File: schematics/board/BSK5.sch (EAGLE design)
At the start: 88 parts, among them U1 STM32F405RGT6, X1 JST-6, X11 JST-6

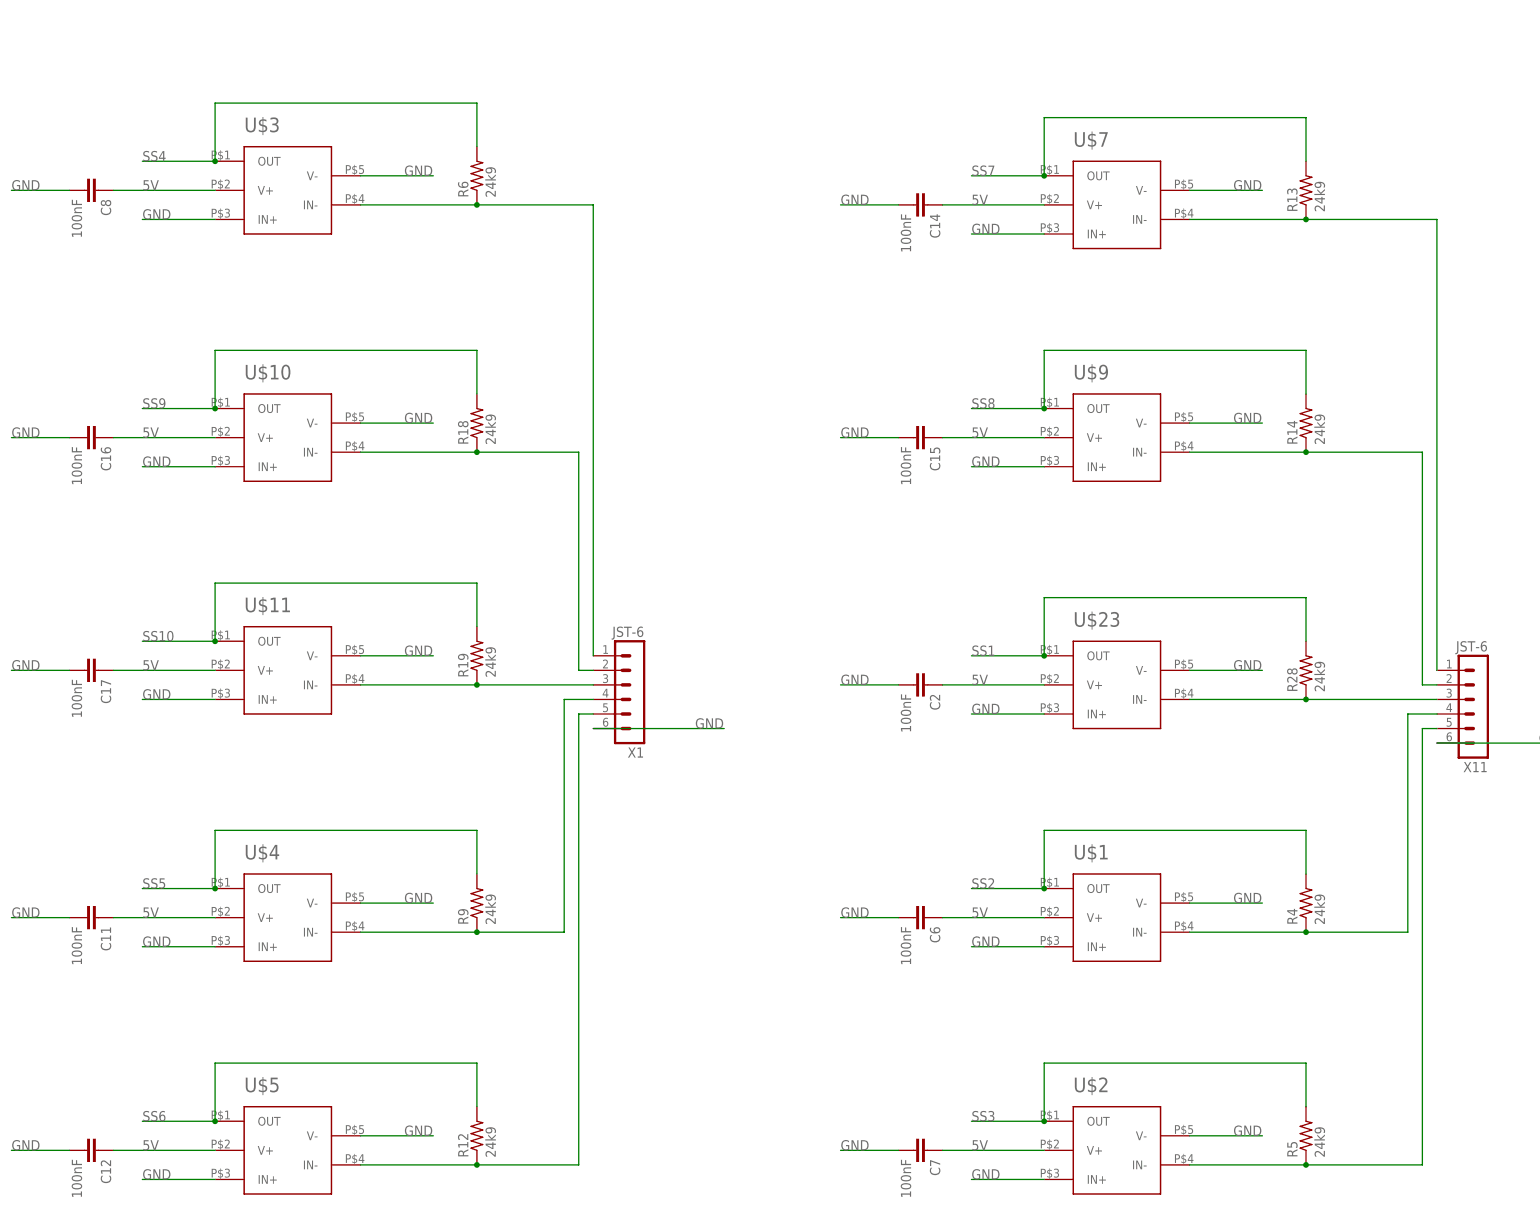
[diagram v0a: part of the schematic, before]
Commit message: Добавлена схема дозиметра, исправлены платы СБ
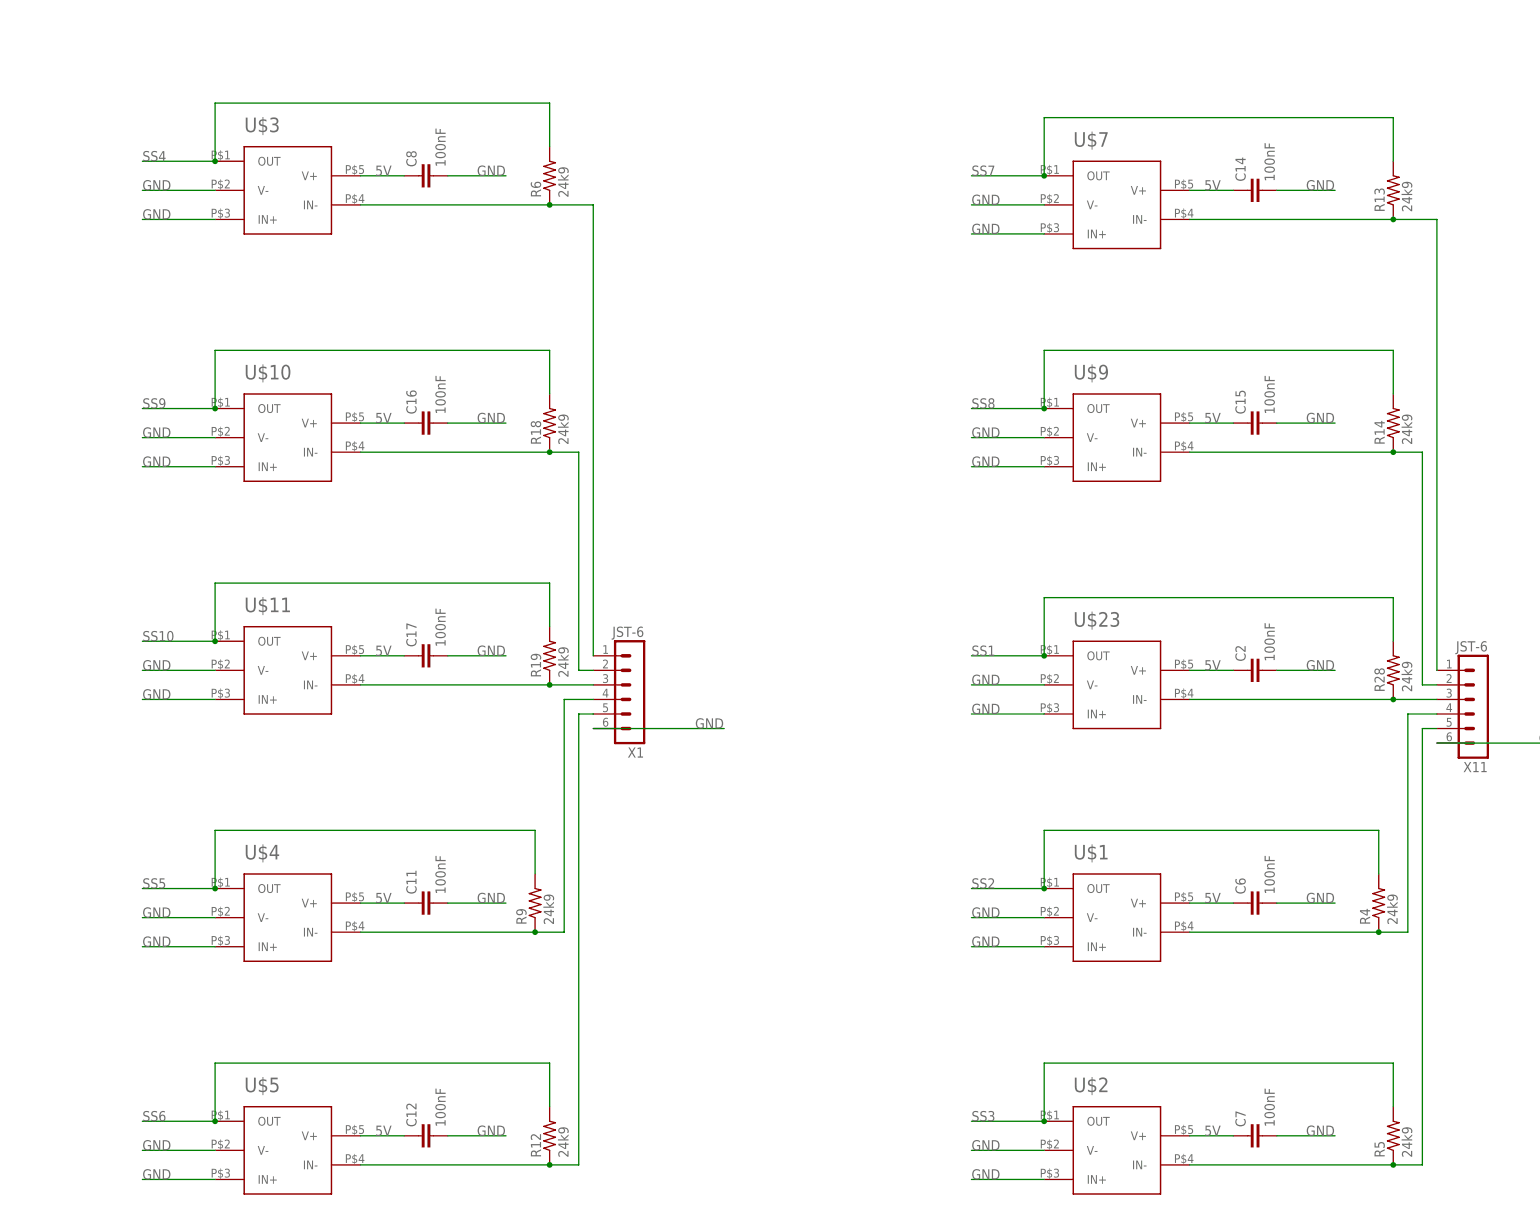
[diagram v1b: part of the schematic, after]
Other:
- moved on the sheet: C11, C12, C14, C15, C16, C17, C2, C6, C7, C8, R12, R13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

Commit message: Схема БКУ
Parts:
- removed U$6: USB-C, CanCubeSat:USB-C
- added U$12: FFC-CONNECT68611, CanCubeSat:FFC-CONNECT68611
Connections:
- net 3V3: now also U$12.1, U$12.2; no longer U$6.3V3/BUS
- net GND: no longer U$6.GND
- net GND-OUT: now also U$12.10, U$12.4, U$12.6, U$12.8
- net NRST: now also U$12.3; no longer U$6.NRST/EN
- net RX-S: now also U$12.5; no longer U$6.RX0
- net SWC: now also U$12.11; no longer U$6.SWC/TXD
- net SWD: now also U$12.9; no longer U$6.SWD/RXD
- net TX-S: now also U$12.7; no longer U$6.TX0
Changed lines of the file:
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@@
 <part name="U1" library="STM32F405RGT6" deviceset="STM32F405RGT6" device=""/>
 <part name="GPS" library="CanCubeSat" deviceset="GPS" device="NEO6M" value="GPSNEO6M"/>
-<part name="U$6" library="CanCubeSat" deviceset="USB-C" device=""/>
 <part name="R1" library="resistor" deviceset="R-US_" device="R0603" package3d_urn="urn:adsk.eagle:package:23555/3" value="10k"/>
 <part name="R15" library="resistor" deviceset="R-US_" device="R0603" package3d_urn="urn:adsk.eagle:package:23555/3" value="2k"/>
@@
 <part name="R31" library="resistor" deviceset="R-US_" device="R0603" package3d_urn="urn:adsk.eagle:package:23555/3" value="100R"/>
 <part name="R32" library="resistor" deviceset="R-US_" device="R0603" package3d_urn="urn:adsk.eagle:package:23555/3" value="100R"/>
+<part name="U$12" library="CanCubeSat" deviceset="FFC-CONNECT" device="68611"/>
 </parts>
 <sheets>
@@
 <attribute name="NAME" x="442.722" y="241.3" size="1.778" layer="95" rot="R270"/>
 </instance>
-<instance part="U$6" gate="G$1" x="88.9" y="264.16" smashed="yes"/>
 <instance part="R1" gate="G$1" x="411.48" y="193.04" smashed="yes" rot="R90">
 <attribute name="NAME" x="409.9814" y="189.23" size="1.778" layer="95" rot="R90"/>
@@
 <attribute name="VALUE" x="519.938" y="306.07" size="1.778" layer="96" rot="R270"/>
 </instance>
+<instance part="U$12" gate="G$1" x="91.44" y="271.78" smashed="yes" rot="R90">
+<attribute name="NAME" x="70.485" y="265.43" size="1.778" layer="95" rot="R90"/>
+<attribute name="VALUE" x="114.3" y="265.43" size="1.778" layer="96" rot="R90"/>
+</instance>
 </instances>
 <busses>
@@
 <nets>
 <net name="GND" class="0">
-<segment>
-<pinref part="U$6" gate="G$1" pin="GND"/>
-<wire x1="71.12" y1="269.24" x2="53.34" y2="269.24" width="0.1524" layer="91"/>
-<label x="53.34" y="269.24" size="1.778" layer="95"/>
-</segment>
 <segment>
 <pinref part="SUPPLY1" gate="GND" pin="GND"/>
@@
 <net name="SWD" class="0">
 <segment>
-<pinref part="U$6" gate="G$1" pin="SWD/RXD"/>
-<wire x1="106.68" y1="269.24" x2="124.46" y2="269.24" width="0.1524" layer="91"/>
-<label x="119.38" y="269.24" size="1.778" layer="95"/>
-</segment>
-<segment>
 <pinref part="U1" gate="G$1" pin="PA13/JMS-SWDIO"/>
 <wire x1="360.68" y1="149.86" x2="421.64" y2="149.86" width="0.1524" layer="91"/>
@@
 <pinref part="R2" gate="G$1" pin="1"/>
 </segment>
+<segment>
+<wire x1="93.98" y1="269.24" x2="93.98" y2="248.92" width="0.1524" layer="91"/>
+<label x="93.98" y="248.92" size="1.778" layer="95" rot="R90"/>
+<pinref part="U$12" gate="G$1" pin="9"/>
+</segment>
 </net>
 <net name="RX-S" class="0">
-<segment>
-<wire x1="53.34" y1="264.16" x2="71.12" y2="264.16" width="0.1524" layer="91"/>
-<label x="53.34" y="264.16" size="1.778" layer="95"/>
-<pinref part="U$6" gate="G$1" pin="RX0"/>
-</segment>
 <segment>
 <pinref part="U1" gate="G$1" pin="PC10"/>
@@
 <label x="487.68" y="157.48" size="1.778" layer="95"/>
 </segment>
+<segment>
+<wire x1="83.82" y1="269.24" x2="83.82" y2="248.92" width="0.1524" layer="91"/>
+<label x="83.82" y="248.92" size="1.778" layer="95" rot="R90"/>
+<pinref part="U$12" gate="G$1" pin="5"/>
+</segment>
 </net>
 <net name="TX-S" class="0">
-<segment>
-<wire x1="124.46" y1="261.62" x2="106.68" y2="261.62" width="0.1524" layer="91"/>
-<label x="119.38" y="261.62" size="1.778" layer="95"/>
-<pinref part="U$6" gate="G$1" pin="TX0"/>
-</segment>
 <segment>
 <pinref part="U1" gate="G$1" pin="PC11"/>
@@
 <label x="487.68" y="154.94" size="1.778" layer="95"/>
 </segment>
+<segment>
+<wire x1="88.9" y1="269.24" x2="88.9" y2="248.92" width="0.1524" layer="91"/>
+<label x="88.9" y="248.92" size="1.778" layer="95" rot="R90"/>
+<pinref part="U$12" gate="G$1" pin="7"/>
+</segment>
 </net>
 <net name="SWC" class="0">
-<segment>
-<wire x1="124.46" y1="266.7" x2="106.68" y2="266.7" width="0.1524" layer="91"/>
-<label x="119.38" y="266.7" size="1.778" layer="95"/>
-<pinref part="U$6" gate="G$1" pin="SWC/TXD"/>
-</segment>
 <segment>
 <pinref part="U1" gate="G$1" pin="PA14/JTCK-SWCLK"/>
@@
 <pinref part="R3" gate="G$1" pin="1"/>
 </segment>
+<segment>
+<wire x1="99.06" y1="269.24" x2="99.06" y2="248.92" width="0.1524" layer="91"/>
+<label x="99.06" y="248.92" size="1.778" layer="95" rot="R90"/>
+<pinref part="U$12" gate="G$1" pin="11"/>
+</segment>
 </net>
 <net name="NRST" class="0">
-<segment>
-<wire x1="53.34" y1="266.7" x2="71.12" y2="266.7" width="0.1524" layer="91"/>
-<label x="53.34" y="266.7" size="1.778" layer="95"/>
-<pinref part="U$6" gate="G$1" pin="NRST/EN"/>
-</segment>
 <segment>
 <pinref part="U1" gate="G$1" pin="NRST"/>
@@
 <junction x="411.48" y="187.96"/>
 <label x="398.78" y="187.96" size="1.778" layer="95"/>
+</segment>
+<segment>
+<pinref part="U$12" gate="G$1" pin="3"/>
+<wire x1="78.74" y1="269.24" x2="78.74" y2="248.92" width="0.1524" layer="91"/>
+<label x="78.74" y="248.92" size="1.778" layer="95" rot="R90"/>
 </segment>
 </net>
@@
 <wire x1="510.54" y1="187.96" x2="482.6" y2="187.96" width="0.1524" layer="91"/>
 <wire x1="482.6" y1="187.96" x2="482.6" y2="195.58" width="0.1524" layer="91"/>
-</segment>
-<segment>
-<wire x1="71.12" y1="261.62" x2="53.34" y2="261.62" width="0.1524" layer="91"/>
-<label x="53.34" y="261.62" size="1.778" layer="95"/>
-<pinref part="U$6" gate="G$1" pin="3V3/BUS"/>
 </segment>
 <segment>
@@
 <label x="551.18" y="121.92" size="1.778" layer="95"/>
 </segment>
+<segment>
+<pinref part="U$12" gate="G$1" pin="2"/>
+<wire x1="76.2" y1="269.24" x2="76.2" y2="248.92" width="0.1524" layer="91"/>
+<label x="76.2" y="248.92" size="1.778" layer="95" rot="R90"/>
+</segment>
+<segment>
+<pinref part="U$12" gate="G$1" pin="1"/>
+<wire x1="73.66" y1="269.24" x2="73.66" y2="248.92" width="0.1524" layer="91"/>
+<label x="73.66" y="248.92" size="1.778" layer="95" rot="R90"/>
+</segment>
 </net>
 <net name="SINS-KVCC" class="0">
@@
 <pinref part="BSK3" gate="A" pin="4"/>
 </segment>
-</net>
+<segment>
+<wire x1="96.52" y1="269.24" x2="96.52" y2="248.92" width="0.1524" layer="91"/>
+<label x="96.52" y="248.92" size="1.778" layer="95" rot="R90"/>
+<pinref part="U$12" gate="G$1" pin="10"/>
+</segment>
+<segment>
+<wire x1="91.44" y1="269.24" x2="91.44" y2="248.92" width="0.1524" layer="91"/>
+<label x="91.44" y="248.92" size="1.778" layer="95" rot="R90"/>
+<pinref part="U$12" gate="G$1" pin="8"/>
+</segment>
+<segment>
+<pinref part="U$12" gate="G$1" pin="6"/>
+<wire x1="86.36" y1="269.24" x2="86.36" y2="248.92" width="0.1524" layer="91"/>
+<label x="86.36" y="248.92" size="1.778" layer="95" rot="R90"/>
+</segment>
+<segment>
+<pinref part="U$12" gate="G$1" pin="4"/>
+<wire x1="81.28" y1="269.24" x2="81.28" y2="248.92" width="0.1524" layer="91"/>
+<label x="81.28" y="248.92" size="1.778" layer="95" rot="R90"/>
+</segment>
+</net>

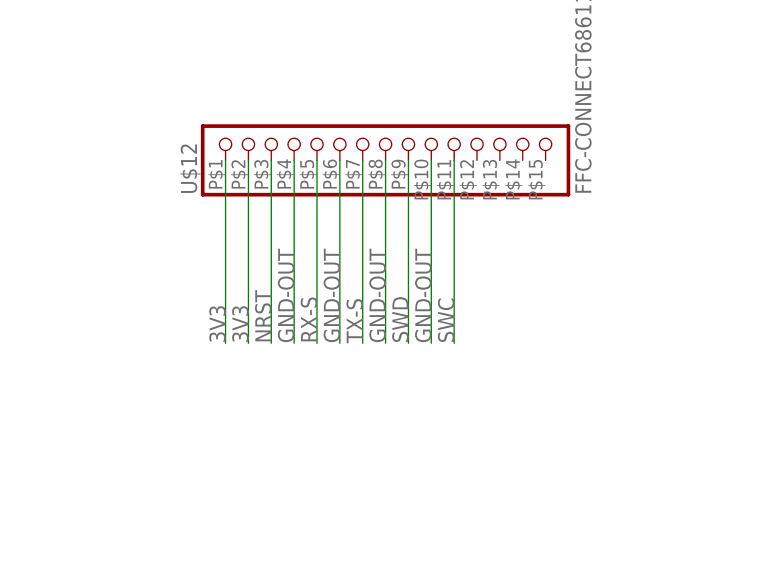
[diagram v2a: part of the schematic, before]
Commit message: Исправлена БСК5
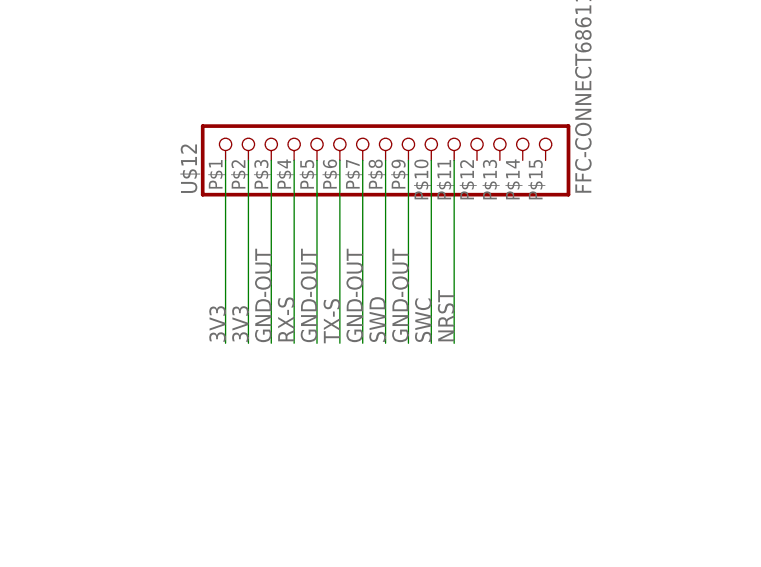
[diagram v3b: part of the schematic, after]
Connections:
- net GND-OUT: now also U$12.3, U$12.5, U$12.7, U$12.9; no longer U$12.10, U$12.4, U$12.6, U$12.8
- net NRST: now also U$12.11; no longer U$12.3
- net RX-S: now also U$12.4; no longer U$12.5
- net SWC: now also U$12.10; no longer U$12.11
- net SWD: now also U$12.8; no longer U$12.9
- net TX-S: now also U$12.6; no longer U$12.7
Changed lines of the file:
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@@
 </segment>
 <segment>
-<wire x1="93.98" y1="269.24" x2="93.98" y2="248.92" width="0.1524" layer="91"/>
-<label x="93.98" y="248.92" size="1.778" layer="95" rot="R90"/>
-<pinref part="U$12" gate="G$1" pin="9"/>
+<wire x1="91.44" y1="269.24" x2="91.44" y2="248.92" width="0.1524" layer="91"/>
+<label x="91.44" y="248.92" size="1.778" layer="95" rot="R90"/>
+<pinref part="U$12" gate="G$1" pin="8"/>
 </segment>
 </net>
@@
 </segment>
 <segment>
-<wire x1="83.82" y1="269.24" x2="83.82" y2="248.92" width="0.1524" layer="91"/>
-<label x="83.82" y="248.92" size="1.778" layer="95" rot="R90"/>
-<pinref part="U$12" gate="G$1" pin="5"/>
+<wire x1="81.28" y1="269.24" x2="81.28" y2="248.92" width="0.1524" layer="91"/>
+<label x="81.28" y="248.92" size="1.778" layer="95" rot="R90"/>
+<pinref part="U$12" gate="G$1" pin="4"/>
 </segment>
 </net>
@@
 </segment>
 <segment>
-<wire x1="88.9" y1="269.24" x2="88.9" y2="248.92" width="0.1524" layer="91"/>
-<label x="88.9" y="248.92" size="1.778" layer="95" rot="R90"/>
-<pinref part="U$12" gate="G$1" pin="7"/>
+<wire x1="86.36" y1="269.24" x2="86.36" y2="248.92" width="0.1524" layer="91"/>
+<label x="86.36" y="248.92" size="1.778" layer="95" rot="R90"/>
+<pinref part="U$12" gate="G$1" pin="6"/>
 </segment>
 </net>
@@
 </segment>
 <segment>
-<wire x1="99.06" y1="269.24" x2="99.06" y2="248.92" width="0.1524" layer="91"/>
-<label x="99.06" y="248.92" size="1.778" layer="95" rot="R90"/>
-<pinref part="U$12" gate="G$1" pin="11"/>
+<wire x1="96.52" y1="269.24" x2="96.52" y2="248.92" width="0.1524" layer="91"/>
+<label x="96.52" y="248.92" size="1.778" layer="95" rot="R90"/>
+<pinref part="U$12" gate="G$1" pin="10"/>
 </segment>
 </net>
@@
 </segment>
 <segment>
-<pinref part="U$12" gate="G$1" pin="3"/>
-<wire x1="78.74" y1="269.24" x2="78.74" y2="248.92" width="0.1524" layer="91"/>
-<label x="78.74" y="248.92" size="1.778" layer="95" rot="R90"/>
+<pinref part="U$12" gate="G$1" pin="11"/>
+<wire x1="99.06" y1="269.24" x2="99.06" y2="248.92" width="0.1524" layer="91"/>
+<label x="99.06" y="248.92" size="1.778" layer="95" rot="R90"/>
 </segment>
 </net>
@@
 </segment>
 <segment>
-<wire x1="96.52" y1="269.24" x2="96.52" y2="248.92" width="0.1524" layer="91"/>
-<label x="96.52" y="248.92" size="1.778" layer="95" rot="R90"/>
-<pinref part="U$12" gate="G$1" pin="10"/>
-</segment>
-<segment>
-<wire x1="91.44" y1="269.24" x2="91.44" y2="248.92" width="0.1524" layer="91"/>
-<label x="91.44" y="248.92" size="1.778" layer="95" rot="R90"/>
-<pinref part="U$12" gate="G$1" pin="8"/>
-</segment>
-<segment>
-<pinref part="U$12" gate="G$1" pin="6"/>
-<wire x1="86.36" y1="269.24" x2="86.36" y2="248.92" width="0.1524" layer="91"/>
-<label x="86.36" y="248.92" size="1.778" layer="95" rot="R90"/>
-</segment>
-<segment>
-<pinref part="U$12" gate="G$1" pin="4"/>
-<wire x1="81.28" y1="269.24" x2="81.28" y2="248.92" width="0.1524" layer="91"/>
-<label x="81.28" y="248.92" size="1.778" layer="95" rot="R90"/>
-</segment>
-</net>
+<wire x1="93.98" y1="269.24" x2="93.98" y2="248.92" width="0.1524" layer="91"/>
+<label x="93.98" y="248.92" size="1.778" layer="95" rot="R90"/>
+<pinref part="U$12" gate="G$1" pin="9"/>
+</segment>
+<segment>
+<wire x1="88.9" y1="269.24" x2="88.9" y2="248.92" width="0.1524" layer="91"/>
+<label x="88.9" y="248.92" size="1.778" layer="95" rot="R90"/>
+<pinref part="U$12" gate="G$1" pin="7"/>
+</segment>
+<segment>
+<wire x1="83.82" y1="269.24" x2="83.82" y2="248.92" width="0.1524" layer="91"/>
+<label x="83.82" y="248.92" size="1.778" layer="95" rot="R90"/>
+<pinref part="U$12" gate="G$1" pin="5"/>
+</segment>
+<segment>
+<wire x1="78.74" y1="269.24" x2="78.74" y2="248.92" width="0.1524" layer="91"/>
+<label x="78.74" y="248.92" size="1.778" layer="95" rot="R90"/>
+<pinref part="U$12" gate="G$1" pin="3"/>
+</segment>
+</net>
